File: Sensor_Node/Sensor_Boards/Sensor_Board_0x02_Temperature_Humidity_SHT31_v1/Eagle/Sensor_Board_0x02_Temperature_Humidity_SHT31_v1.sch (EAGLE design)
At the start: 15 parts, among them J1 M04_SMD_90, J2 M07_SMD_STRAIGHT, J4 ARDUINO_ISP, U2 ATMEGA328P_TQFP, Y1 8MHZ

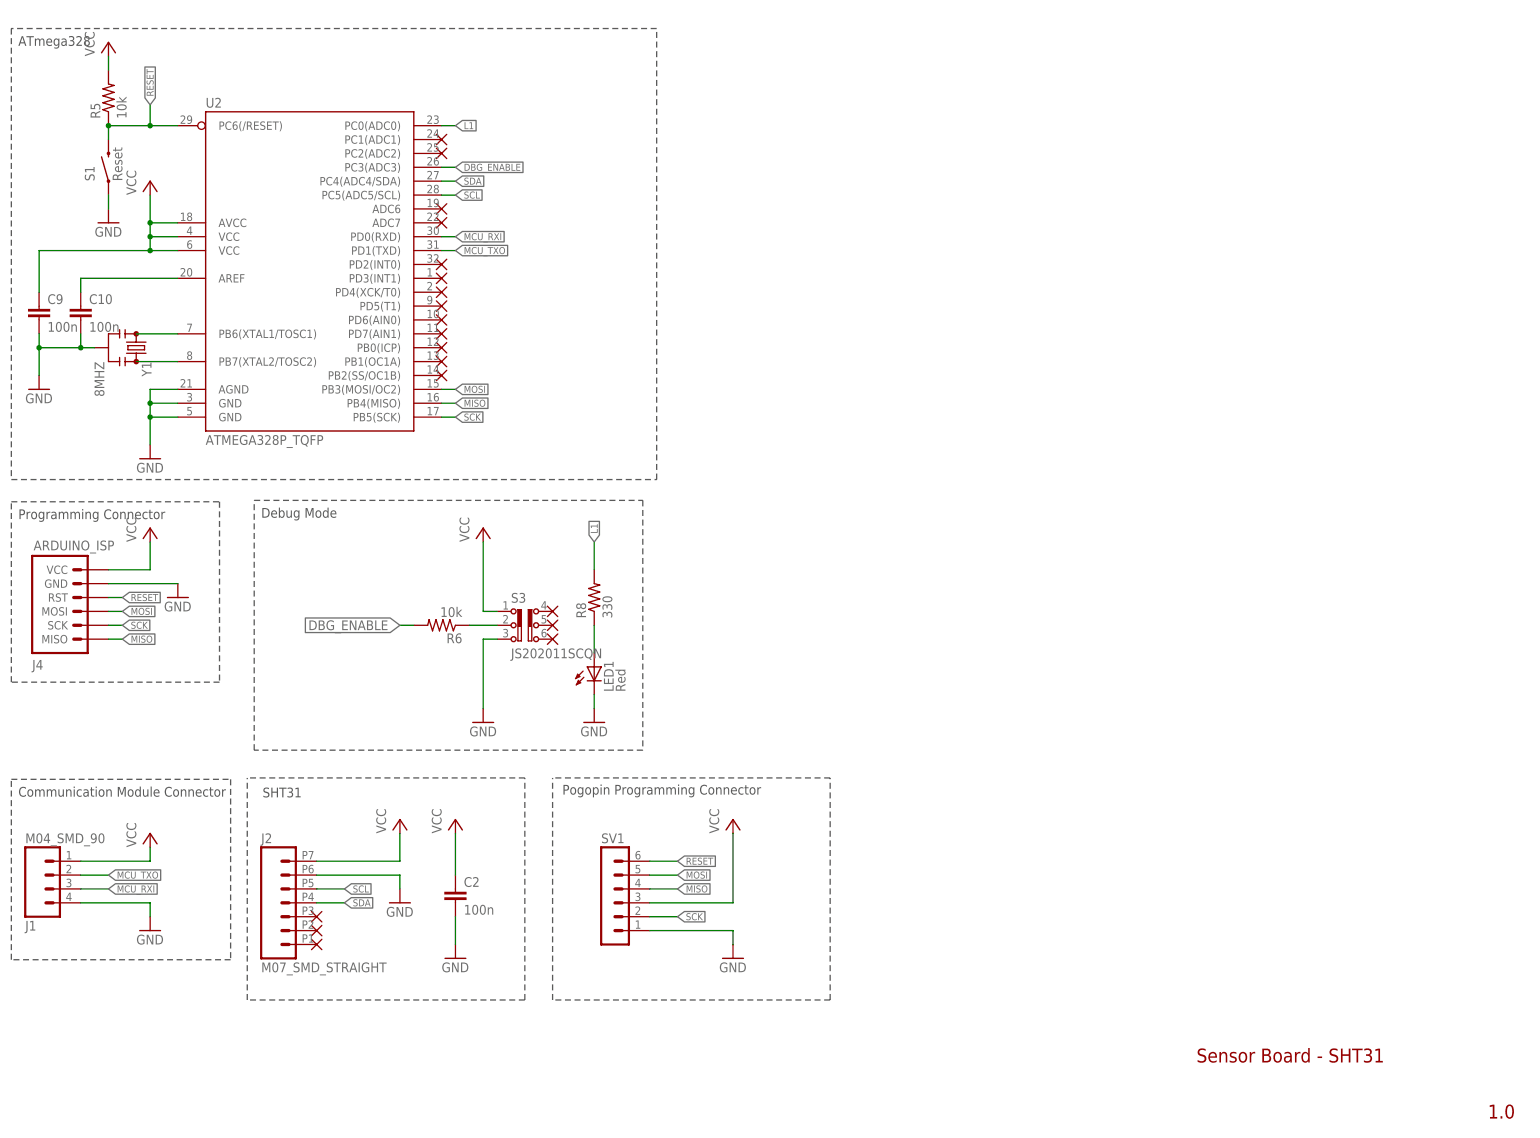
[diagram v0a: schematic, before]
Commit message: Changes on all boards
- added capacitor on reset-path
- changed order of pogopin programmer pins

Pulse-Board:
- Deleted input-jumper. Currently one interrupt-pin missing, so print is
not yet routed.
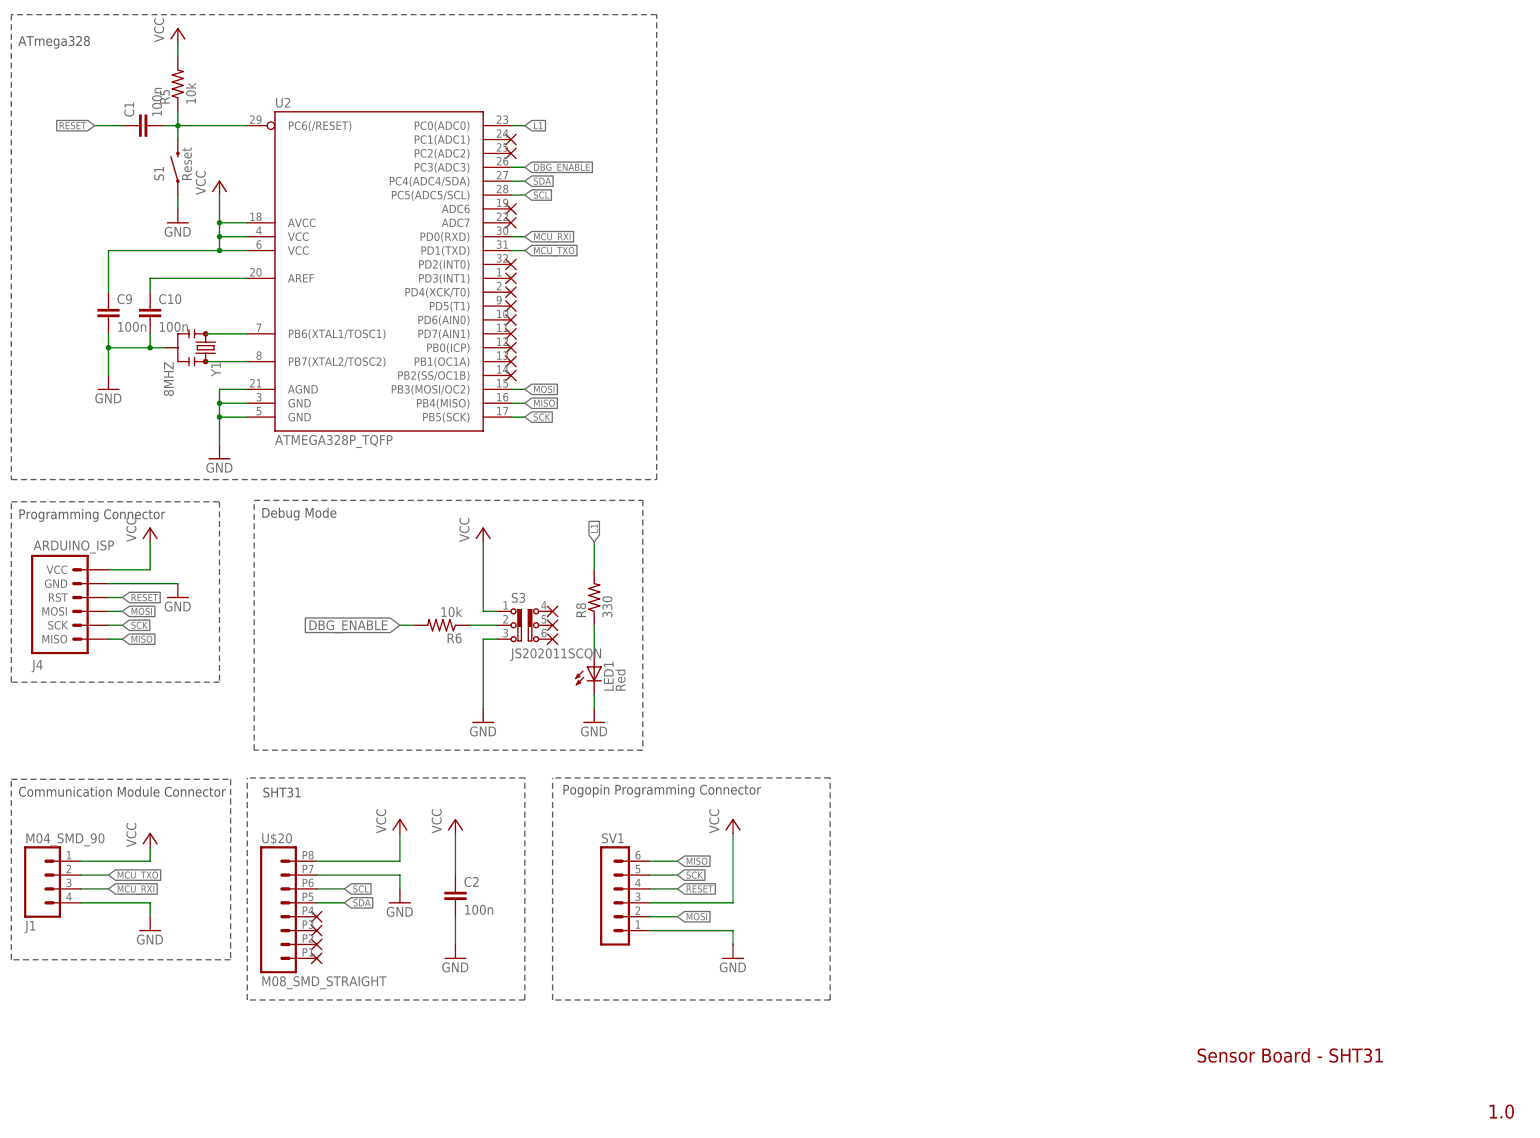
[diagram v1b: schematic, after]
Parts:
- removed J2: M07_SMD_STRAIGHT, myownthings:M07_SMD_STRAIGHT
- added C1: 100n, eagle-ltspice:C
- added U$20: M08_SMD_STRAIGHT, myownthings:M08_SMD_STRAIGHT
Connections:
- new net N$4: C1.2, R5.1, S1.RIGHT, U2.PC6(/RESET)
- net GND: now also U$20.7; no longer J2.6
- net MISO: now also SV1.6; no longer SV1.4
- net MOSI: now also SV1.2; no longer SV1.5
- net RESET: now also C1.1, SV1.4; no longer R5.1, S1.RIGHT, SV1.6, U2.PC6(/RESET)
- net SCK: now also SV1.5; no longer SV1.2
- net SCL: now also U$20.6; no longer J2.5
- net SDA: now also U$20.5; no longer J2.4
- net VCC: now also U$20.8; no longer J2.7
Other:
- moved on the sheet: C10, C9, R5, S1, U2, Y1

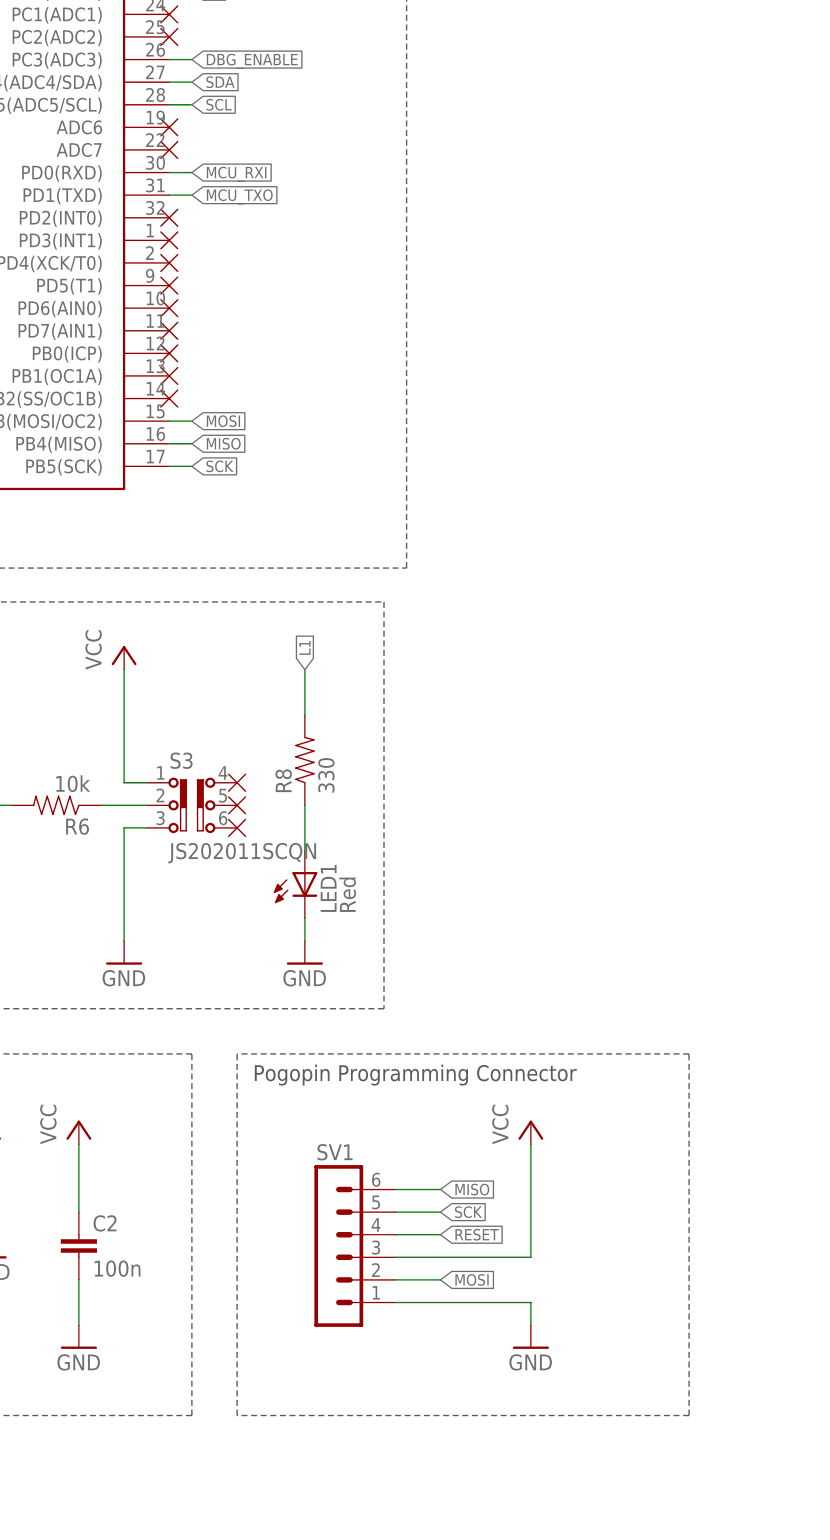
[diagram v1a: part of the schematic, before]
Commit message: Changed SensorBoard SHT31
- changed pogopin-programmer to FTDI
- connection with comboard is now over software serial instead of
hardware serial
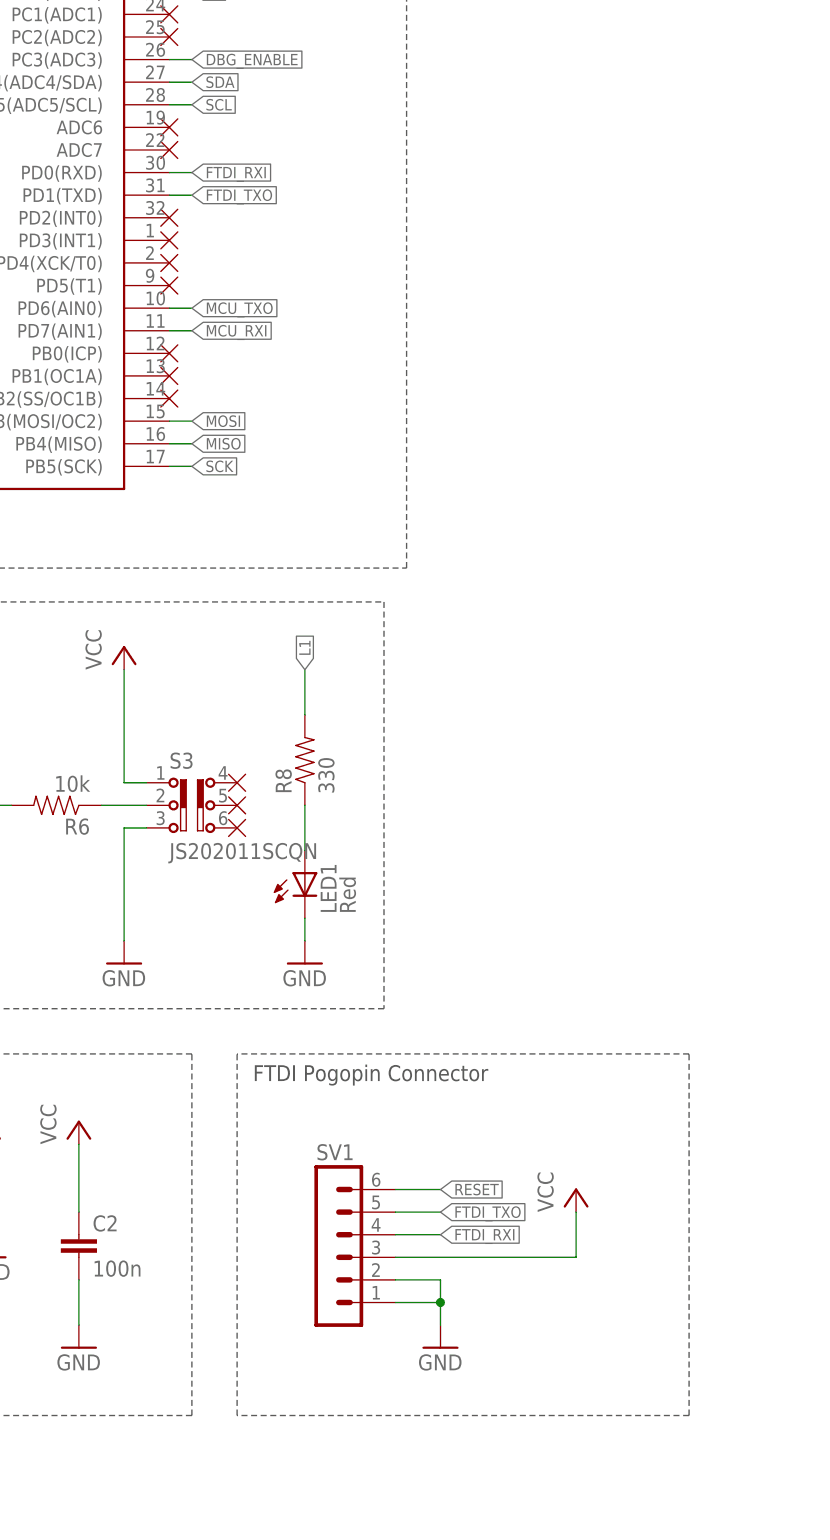
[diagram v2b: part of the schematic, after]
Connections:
- new net FTDI_RXI: SV1.4, U2.PD0(RXD)
- new net FTDI_TXO: SV1.5, U2.PD1(TXD)
- net GND: now also SV1.2
- net MCU_RXI: now also U2.PD7(AIN1); no longer U2.PD0(RXD)
- net MCU_TXO: now also U2.PD6(AIN0); no longer U2.PD1(TXD)
- net MISO: no longer SV1.6
- net MOSI: no longer SV1.2
- net RESET: now also SV1.6; no longer SV1.4
- net SCK: no longer SV1.5
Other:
- note added: "FTDI Pogopin Connector"
- note removed: "Pogopin Programming Connector"
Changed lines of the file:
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@@
 <part name="P+15" library="supply1" deviceset="VCC" device=""/>
 <part name="S3" library="myownthings" deviceset="JS202011SCQN" device=""/>
-<part name="U$1" library="myownthings" deviceset="N/C" device=""/>
-<part name="U$2" library="myownthings" deviceset="N/C" device=""/>
 <part name="U$3" library="myownthings" deviceset="N/C" device=""/>
 <part name="U$4" library="myownthings" deviceset="N/C" device=""/>
@@
 <part name="U$7" library="myownthings" deviceset="N/C" device=""/>
 <part name="U$8" library="myownthings" deviceset="N/C" device=""/>
-<part name="U$9" library="myownthings" deviceset="N/C" device=""/>
-<part name="U$10" library="myownthings" deviceset="N/C" device=""/>
 <part name="U$11" library="myownthings" deviceset="N/C" device=""/>
 <part name="U$12" library="myownthings" deviceset="N/C" device=""/>
@@
 <part name="U$20" library="myownthings" deviceset="M08_SMD_STRAIGHT" device=""/>
 <part name="U$21" library="myownthings" deviceset="N/C" device=""/>
+<part name="U$1" library="myownthings" deviceset="N/C" device=""/>
+<part name="U$2" library="myownthings" deviceset="N/C" device=""/>
 </parts>
 <sheets>
@@
 <wire x1="106.68" y1="22.86" x2="106.68" y2="63.5" width="0.1524" layer="97" style="shortdash"/>
 <wire x1="157.48" y1="22.86" x2="157.48" y2="63.5" width="0.1524" layer="97" style="shortdash"/>
-<text x="108.458" y="60.452" size="1.778" layer="97">Pogopin Programming Connector</text>
+<text x="108.458" y="60.452" size="1.778" layer="97">FTDI Pogopin Connector</text>
 </plain>
 <instances>
@@
 <instance part="P+15" gate="VCC" x="88.9" y="55.88"/>
 <instance part="S3" gate="G$1" x="101.6" y="91.44"/>
-<instance part="U$1" gate="G$1" x="99.06" y="180.34"/>
-<instance part="U$2" gate="G$1" x="99.06" y="177.8"/>
 <instance part="U$3" gate="G$1" x="99.06" y="167.64"/>
 <instance part="U$4" gate="G$1" x="99.06" y="165.1"/>
@@
 <instance part="U$7" gate="G$1" x="99.06" y="149.86"/>
 <instance part="U$8" gate="G$1" x="99.06" y="152.4"/>
-<instance part="U$9" gate="G$1" x="99.06" y="147.32"/>
-<instance part="U$10" gate="G$1" x="99.06" y="144.78"/>
 <instance part="U$11" gate="G$1" x="99.06" y="142.24"/>
 <instance part="U$12" gate="G$1" x="99.06" y="139.7"/>
@@
 <instance part="U$19" gate="G$1" x="63.5" y="33.02"/>
 <instance part="SV1" gate="1" x="116.84" y="43.18"/>
-<instance part="GND1" gate="1" x="139.7" y="30.48"/>
-<instance part="P+6" gate="VCC" x="139.7" y="55.88"/>
+<instance part="GND1" gate="1" x="129.54" y="30.48"/>
+<instance part="P+6" gate="VCC" x="144.78" y="48.26"/>
 <instance part="C1" gate="G$1" x="30.48" y="182.88" rot="R90"/>
 <instance part="U$20" gate="G$1" x="58.42" y="35.56"/>
 <instance part="U$21" gate="G$1" x="63.5" y="30.48"/>
+<instance part="U$1" gate="G$1" x="99.06" y="180.34"/>
+<instance part="U$2" gate="G$1" x="99.06" y="177.8"/>
 </instances>
 <busses>
@@
 <pinref part="SV1" gate="1" pin="1"/>
 <pinref part="GND1" gate="1" pin="GND"/>
-<wire x1="124.46" y1="35.56" x2="139.7" y2="35.56" width="0.1524" layer="91"/>
-<wire x1="139.7" y1="35.56" x2="139.7" y2="33.02" width="0.1524" layer="91"/>
+<wire x1="124.46" y1="35.56" x2="129.54" y2="35.56" width="0.1524" layer="91"/>
+<wire x1="129.54" y1="35.56" x2="129.54" y2="33.02" width="0.1524" layer="91"/>
+<pinref part="SV1" gate="1" pin="2"/>
+<wire x1="124.46" y1="38.1" x2="129.54" y2="38.1" width="0.1524" layer="91"/>
+<wire x1="129.54" y1="38.1" x2="129.54" y2="35.56" width="0.1524" layer="91"/>
+<junction x="129.54" y="35.56"/>
 </segment>
 </net>
@@
 <pinref part="SV1" gate="1" pin="3"/>
 <pinref part="P+6" gate="VCC" pin="VCC"/>
-<wire x1="124.46" y1="40.64" x2="139.7" y2="40.64" width="0.1524" layer="91"/>
-<wire x1="139.7" y1="40.64" x2="139.7" y2="53.34" width="0.1524" layer="91"/>
+<wire x1="124.46" y1="40.64" x2="144.78" y2="40.64" width="0.1524" layer="91"/>
+<wire x1="144.78" y1="40.64" x2="144.78" y2="45.72" width="0.1524" layer="91"/>
 </segment>
 </net>
@@
 </segment>
 <segment>
-<pinref part="SV1" gate="1" pin="4"/>
-<wire x1="124.46" y1="43.18" x2="129.54" y2="43.18" width="0.1524" layer="91"/>
-<label x="129.54" y="43.18" size="1.27" layer="95" xref="yes"/>
+<pinref part="SV1" gate="1" pin="6"/>
+<wire x1="124.46" y1="48.26" x2="129.54" y2="48.26" width="0.1524" layer="91"/>
+<label x="129.54" y="48.26" size="1.27" layer="95" xref="yes"/>
 </segment>
 </net>
@@
 <pinref part="U2" gate="U$1" pin="PB5(SCK)"/>
 </segment>
-<segment>
-<pinref part="SV1" gate="1" pin="5"/>
-<wire x1="124.46" y1="45.72" x2="129.54" y2="45.72" width="0.1524" layer="91"/>
-<label x="129.54" y="45.72" size="1.27" layer="95" xref="yes"/>
-</segment>
 </net>
 <net name="MISO" class="0">
@@
 <pinref part="U2" gate="U$1" pin="PB4(MISO)"/>
 </segment>
-<segment>
-<pinref part="SV1" gate="1" pin="6"/>
-<wire x1="124.46" y1="48.26" x2="129.54" y2="48.26" width="0.1524" layer="91"/>
-<label x="129.54" y="48.26" size="1.27" layer="95" xref="yes"/>
-</segment>
 </net>
 <net name="MOSI" class="0">
@@
 <pinref part="U2" gate="U$1" pin="PB3(MOSI/OC2)"/>
 </segment>
-<segment>
-<pinref part="SV1" gate="1" pin="2"/>
-<wire x1="124.46" y1="38.1" x2="129.54" y2="38.1" width="0.1524" layer="91"/>
-<label x="129.54" y="38.1" size="1.27" layer="95" xref="yes"/>
-</segment>
 </net>
 <net name="MCU_TXO" class="0">
-<segment>
-<wire x1="99.06" y1="160.02" x2="101.6" y2="160.02" width="0.1524" layer="91"/>
-<label x="101.6" y="160.02" size="1.27" layer="95" xref="yes"/>
-<pinref part="U2" gate="U$1" pin="PD1(TXD)"/>
-</segment>
 <segment>
 <wire x1="20.32" y1="45.72" x2="25.4" y2="45.72" width="0.1524" layer="91"/>
@@
 <pinref part="J1" gate="G$1" pin="2"/>
 </segment>
+<segment>
+<pinref part="U2" gate="U$1" pin="PD6(AIN0)"/>
+<wire x1="99.06" y1="147.32" x2="101.6" y2="147.32" width="0.1524" layer="91"/>
+<label x="101.6" y="147.32" size="1.27" layer="95" xref="yes"/>
+</segment>
 </net>
 <net name="SCL" class="0">
@@
 <net name="MCU_RXI" class="0">
 <segment>
-<wire x1="99.06" y1="162.56" x2="101.6" y2="162.56" width="0.1524" layer="91"/>
-<label x="101.6" y="162.56" size="1.27" layer="95" xref="yes"/>
-<pinref part="U2" gate="U$1" pin="PD0(RXD)"/>
-</segment>
-<segment>
 <wire x1="20.32" y1="43.18" x2="25.4" y2="43.18" width="0.1524" layer="91"/>
 <label x="25.4" y="43.18" size="1.27" layer="95" xref="yes"/>
 <pinref part="J1" gate="G$1" pin="3"/>
+</segment>
+<segment>
+<pinref part="U2" gate="U$1" pin="PD7(AIN1)"/>
+<wire x1="99.06" y1="144.78" x2="101.6" y2="144.78" width="0.1524" layer="91"/>
+<label x="101.6" y="144.78" size="1.27" layer="95" xref="yes"/>
 </segment>
 </net>
@@
 </segment>
 </net>
+<net name="FTDI_TXO" class="0">
+<segment>
+<pinref part="SV1" gate="1" pin="5"/>
+<wire x1="124.46" y1="45.72" x2="129.54" y2="45.72" width="0.1524" layer="91"/>
+<label x="129.54" y="45.72" size="1.27" layer="95" xref="yes"/>
+</segment>
+<segment>
+<wire x1="99.06" y1="160.02" x2="101.6" y2="160.02" width="0.1524" layer="91"/>
+<label x="101.6" y="160.02" size="1.27" layer="95" xref="yes"/>
+<pinref part="U2" gate="U$1" pin="PD1(TXD)"/>
+</segment>
+</net>
+<net name="FTDI_RXI" class="0">
+<segment>
+<pinref part="SV1" gate="1" pin="4"/>
+<wire x1="124.46" y1="43.18" x2="129.54" y2="43.18" width="0.1524" layer="91"/>
+<label x="129.54" y="43.18" size="1.27" layer="95" xref="yes"/>
+</segment>
+<segment>
+<wire x1="99.06" y1="162.56" x2="101.6" y2="162.56" width="0.1524" layer="91"/>
+<label x="101.6" y="162.56" size="1.27" layer="95" xref="yes"/>
+<pinref part="U2" gate="U$1" pin="PD0(RXD)"/>
+</segment>
+</net>
